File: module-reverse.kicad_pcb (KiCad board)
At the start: 2 copper layers, 99 x 84.2 mm, 18 parts, among them J1 Screw_Terminal_01x02, J10 Screw_Terminal_01x05, J11 Screw_Terminal_01x05, J2 Screw_Terminal_01x02, J7 Screw_Terminal_01x02, J8 Screw_Terminal_01x02, J9 Screw_Terminal_01x02, K1 AZ733-2CE-12DE, U1 L7812

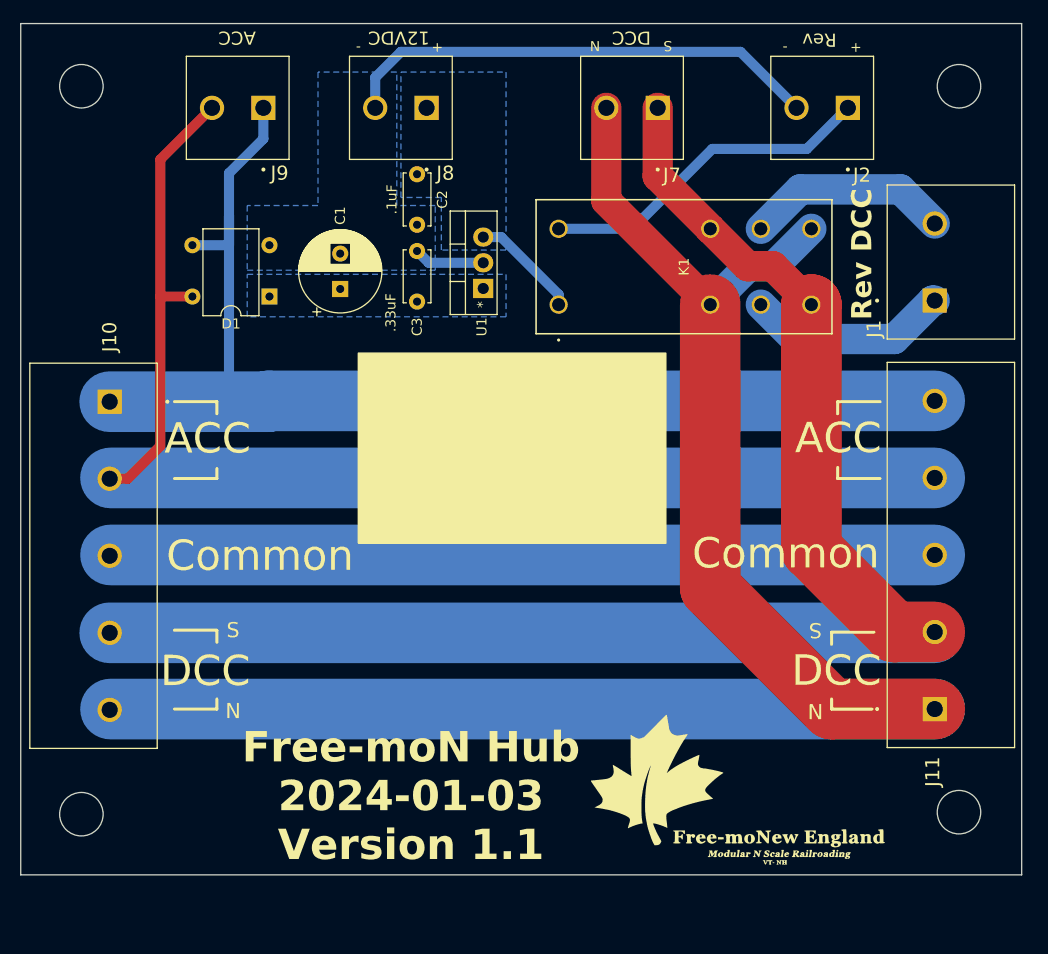
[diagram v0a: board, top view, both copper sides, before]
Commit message: Changed the reversing output to have both Normal and Reverse outputs that go to the two branches instead of a single output that reverses.
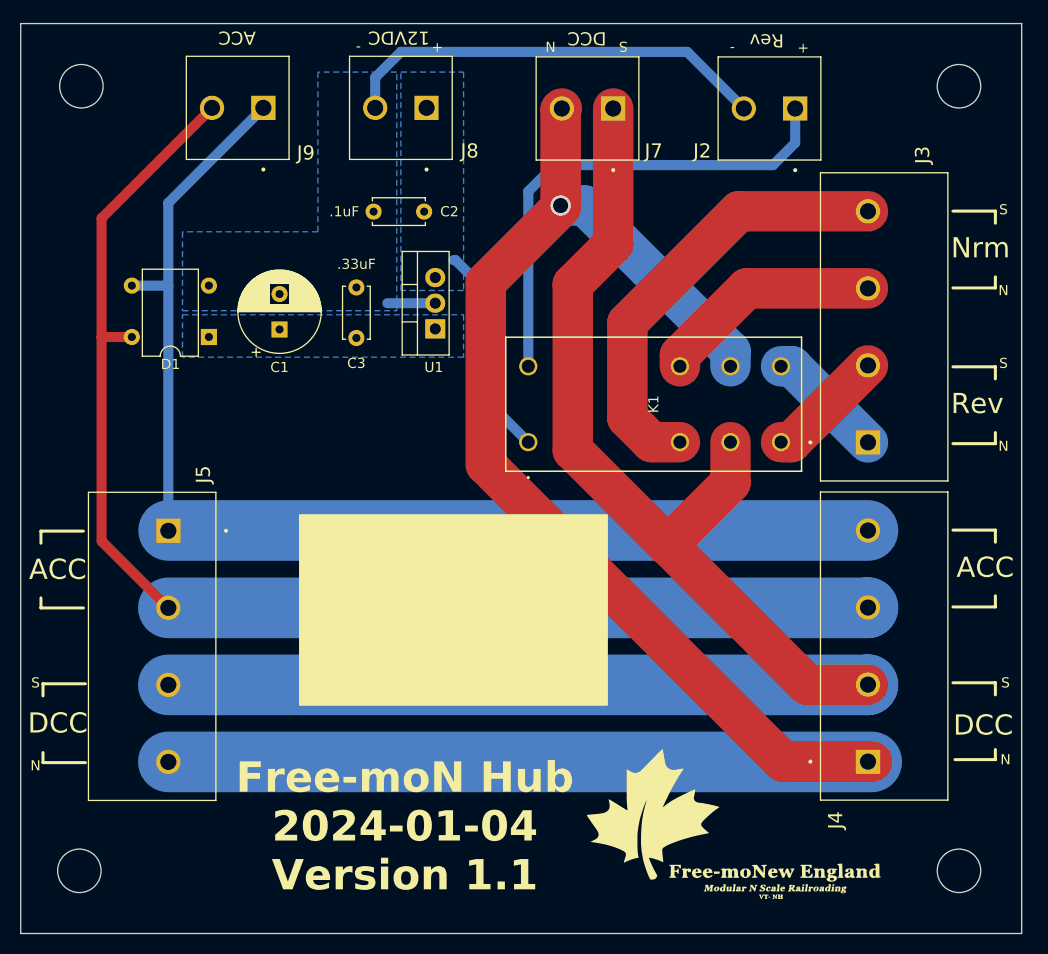
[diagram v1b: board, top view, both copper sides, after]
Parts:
- removed J1: Screw_Terminal_01x02, Imports:CUI_TB005-762-02BE
- removed J10, J11: Screw_Terminal_01x05, Imports:CUI_TB005-762-05BE
- added J3: Screw_Terminal_01x04, Imports:CUI_TB005-762-04BE, F.Cu at (183.8, 91.2)
- added J4: Screw_Terminal_01x04, Imports:CUI_TB005-762-04BE, F.Cu at (183.8, 122.8)
- added J5: Screw_Terminal_01x04, Imports:CUI_TB005-762-04BE, F.Cu at (114.6, 100.0)
- moved K1 13.9 mm to (150.2, 91.2)
- moved C1 7.21 mm to (125.6, 80.1)
- moved D1 7.20 mm to (118.6, 80.8)
- moved C3 7.00 mm to (133.2, 80.9)
- moved U1 6.21 mm to (141.0, 80.0)
- moved REF** 5.80 mm to (192.8, 133.6)
- moved REF** 5.60 mm to (105.8, 133.6)
- moved J2 5.21 mm to (176.6, 58.2)
- moved J7 4.40 mm to (158.6, 58.2)
- moved C2 3.77 mm to (139.9, 68.4), turned to 180 degrees
- moved G*** 3.42 mm to (170.4, 129.4)
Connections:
- J7 pad 1: Net-(J10-Pin_4) -> Net-(J4-Pin_2)
- J7 pad 2: Net-(J10-Pin_5) -> Net-(J4-Pin_1)
- K1 pad 2: Net-(J10-Pin_5) -> Net-(J3-Pin_4)
- K1 pad 3: Net-(J1-Pin_1) -> Net-(J4-Pin_2)
- K1 pad 4: Net-(J10-Pin_4) -> Net-(J3-Pin_2)
- K1 pad 5: Net-(J10-Pin_5) -> Net-(J3-Pin_1)
- K1 pad 6: Net-(J1-Pin_2) -> Net-(J4-Pin_1)
- K1 pad 7: Net-(J10-Pin_4) -> Net-(J3-Pin_3)
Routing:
- net Net-(J4-Pin_1): track 0.00 -> 182.5 mm, vias 0 -> 1
- net Net-(J10-Pin_5): track 173.5 -> 0.00 mm
- net Net-(J4-Pin_2): track 0.00 -> 156.2 mm
- net Net-(J10-Pin_4): track 148.5 -> 0.00 mm
- net Net-(J10-Pin_3): track 81.5 -> 0.00 mm
- net Net-(J3-Pin_4): track 0.00 -> 44.0 mm
- net Net-(J3-Pin_3): track 0.00 -> 22.4 mm
- net Net-(J1-Pin_2): track 20.2 -> 0.00 mm
- net Net-(J1-Pin_1): track 20.2 -> 0.00 mm
- net Net-(J2-Pin_1): track 33.6 -> 49.1 mm
- net Net-(J3-Pin_2): track 0.00 -> 11.7 mm
- net Net-(J3-Pin_1): track 0.00 -> 11.7 mm
- net /+12V: track 10.8 -> 21.2 mm
- net /-12V: track 55.6 -> 47.7 mm
- net Net-(J4-Pin_3): track 126.4 -> 128.9 mm
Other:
- board size 99 x 84.2 mm -> 99 x 90 mm

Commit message: Added LEDs
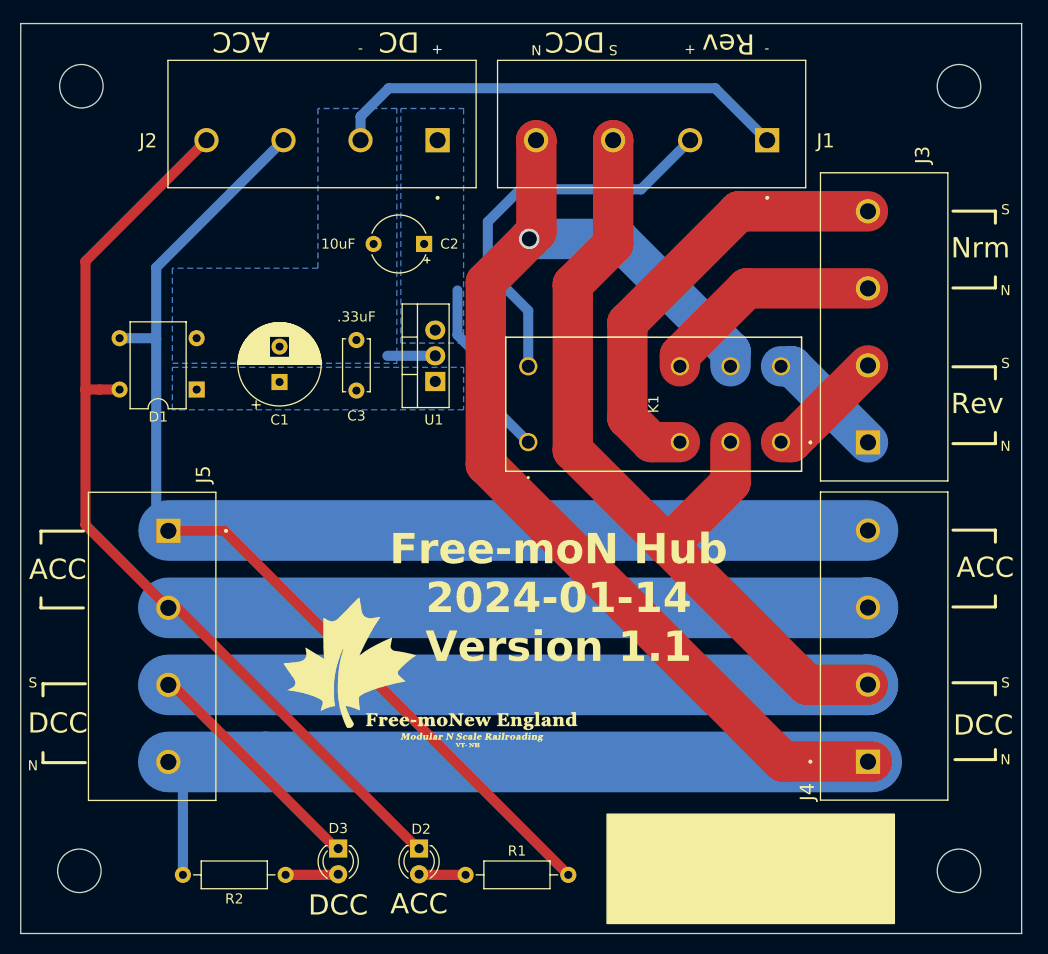
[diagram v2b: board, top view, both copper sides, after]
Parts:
- removed J7, J8, J9: Screw_Terminal_01x02, Imports:CUI_TB004-508-02BE
- added D2: Green, LED_THT:LED_D3.0mm, F.Cu at (139.4, 131.4)
- added D3: Green, LED_THT:LED_D3.0mm, F.Cu at (131.4, 131.4)
- added J1: Screw_Terminal_01x04, Imports:CUI_TB005-762-04BE, F.Cu at (173.8, 61.3)
- added R1: 2.7k, Resistor_THT:R_Axial_DIN0207_L6.3mm_D2.5mm_P10.16mm_Horizontal, F.Cu at (144.0, 134.0)
- added R2: 2.7k, Resistor_THT:R_Axial_DIN0207_L6.3mm_D2.5mm_P10.16mm_Horizontal, F.Cu at (126.2, 134.0)
- C2: value .1uF -> 10uF; footprint Capacitor_THT:C_Disc_D5.0mm_W2.5mm_P5.00mm -> Capacitor_THT:CP_Radial_Tantal_D5.5mm_P5.00mm
- J2: value Screw_Terminal_01x02 -> Screw_Terminal_01x04; footprint Imports:CUI_TB004-508-02BE -> Imports:CUI_TB005-762-04BE
- U1: value L7812 -> 12V
- moved J2 35.5 mm to (141.2, 61.3)
- moved G*** 33.5 mm to (140.4, 114.4)
- moved D1 5.34 mm to (117.4, 86.0)
- moved C1 5.20 mm to (125.6, 85.3)
- moved U1 5.20 mm to (141.0, 85.2)
- moved C3 5.20 mm to (133.2, 86.1)
- moved C2 3.20 mm to (139.9, 71.6)
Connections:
- D1 pad 3: Net-(J4-Pin_4) -> Net-(J2-Pin_3)
- D1 pad 4: Net-(J4-Pin_3) -> Net-(D2-K)
- J2 pad 1: Net-(J2-Pin_1) -> /+12V
- J4 pad 3: Net-(J4-Pin_3) -> Net-(D2-K)
- J4 pad 4: Net-(J4-Pin_4) -> Net-(J2-Pin_3)
- J5 pad 1: Net-(J4-Pin_4) -> Net-(J2-Pin_3)
- J5 pad 2: Net-(J4-Pin_3) -> Net-(D2-K)
- K1 pad 8: Net-(J2-Pin_1) -> Net-(J1-Pin_2)
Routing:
- net Net-(J2-Pin_3): track 0.00 -> 170.8 mm
- net Net-(D2-K): track 0.00 -> 161.9 mm
- net Net-(J4-Pin_3): track 128.9 -> 0.00 mm
- net Net-(J4-Pin_4): track 118.5 -> 0.00 mm
- net Net-(J2-Pin_1): track 49.1 -> 0.00 mm
- net Net-(J1-Pin_2): track 0.00 -> 39.3 mm
- net Net-(D3-K): track 156.2 -> 176.6 mm
- net Net-(J1-Pin_4): track 182.5 -> 191.9 mm
- net Net-(D3-A): track 0.00 -> 5.06 mm
- net Net-(D2-A): track 0.00 -> 4.62 mm
- net /+12V: track 21.2 -> 17.9 mm
- net /-12V: track 47.7 -> 50.6 mm

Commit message: Updated reelase date and produced files for v1.1
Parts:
- removed the G*** at (140.4, 114.4)
- added G***: LOGO, myMods:Free-moNH-40, F.Cu at (142.5, 113.1)
